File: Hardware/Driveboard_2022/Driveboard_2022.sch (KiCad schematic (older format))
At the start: 98 parts

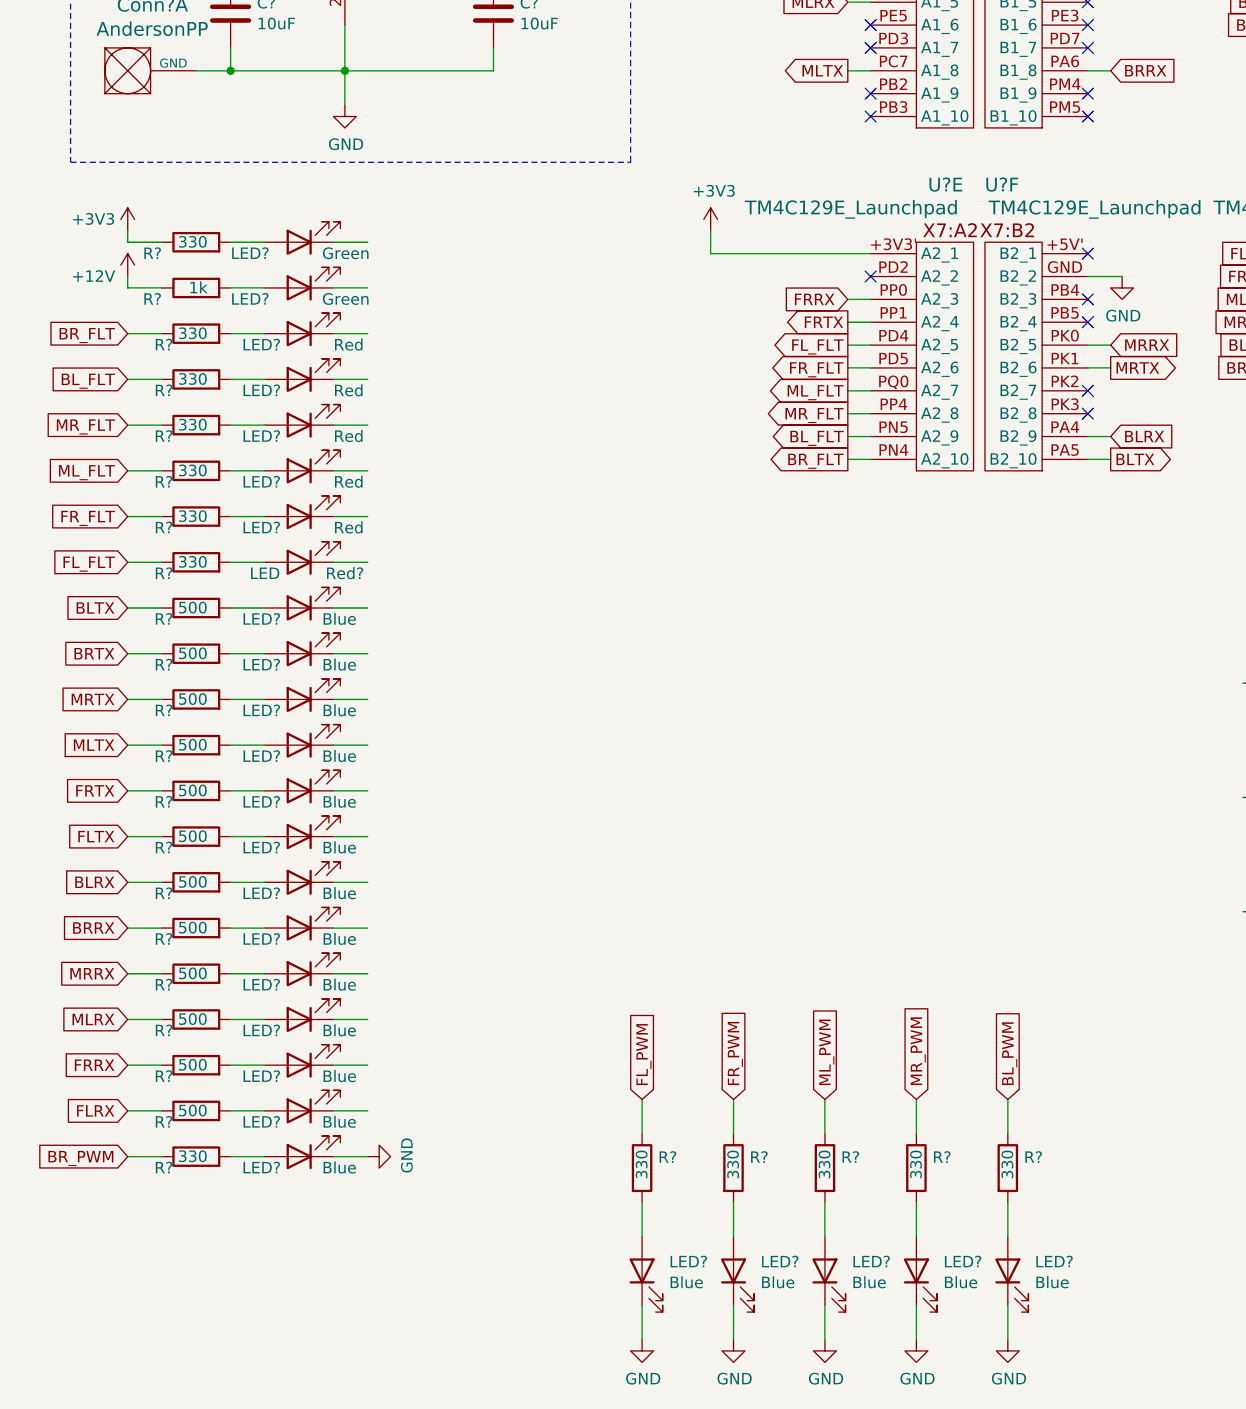
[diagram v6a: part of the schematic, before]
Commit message: Finished Organizing LEDs
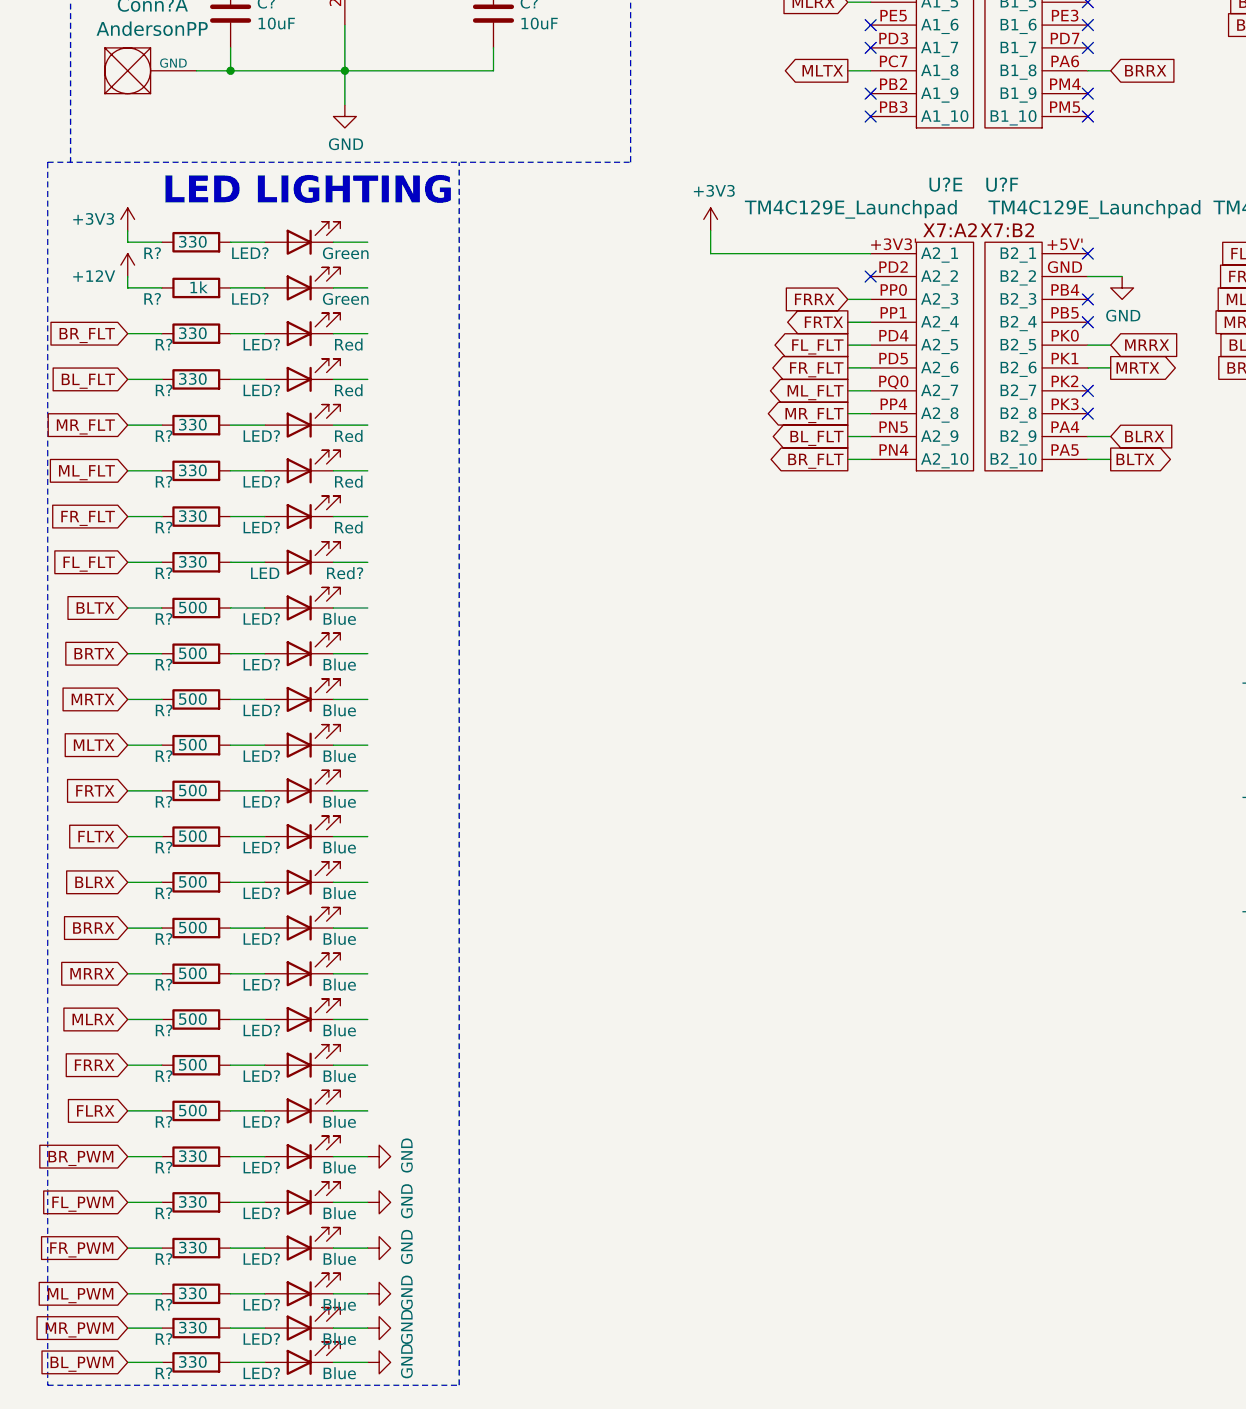
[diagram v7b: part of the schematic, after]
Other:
- note added: "LED LIGHTING\n"
- moved on the sheet: LED?, R?

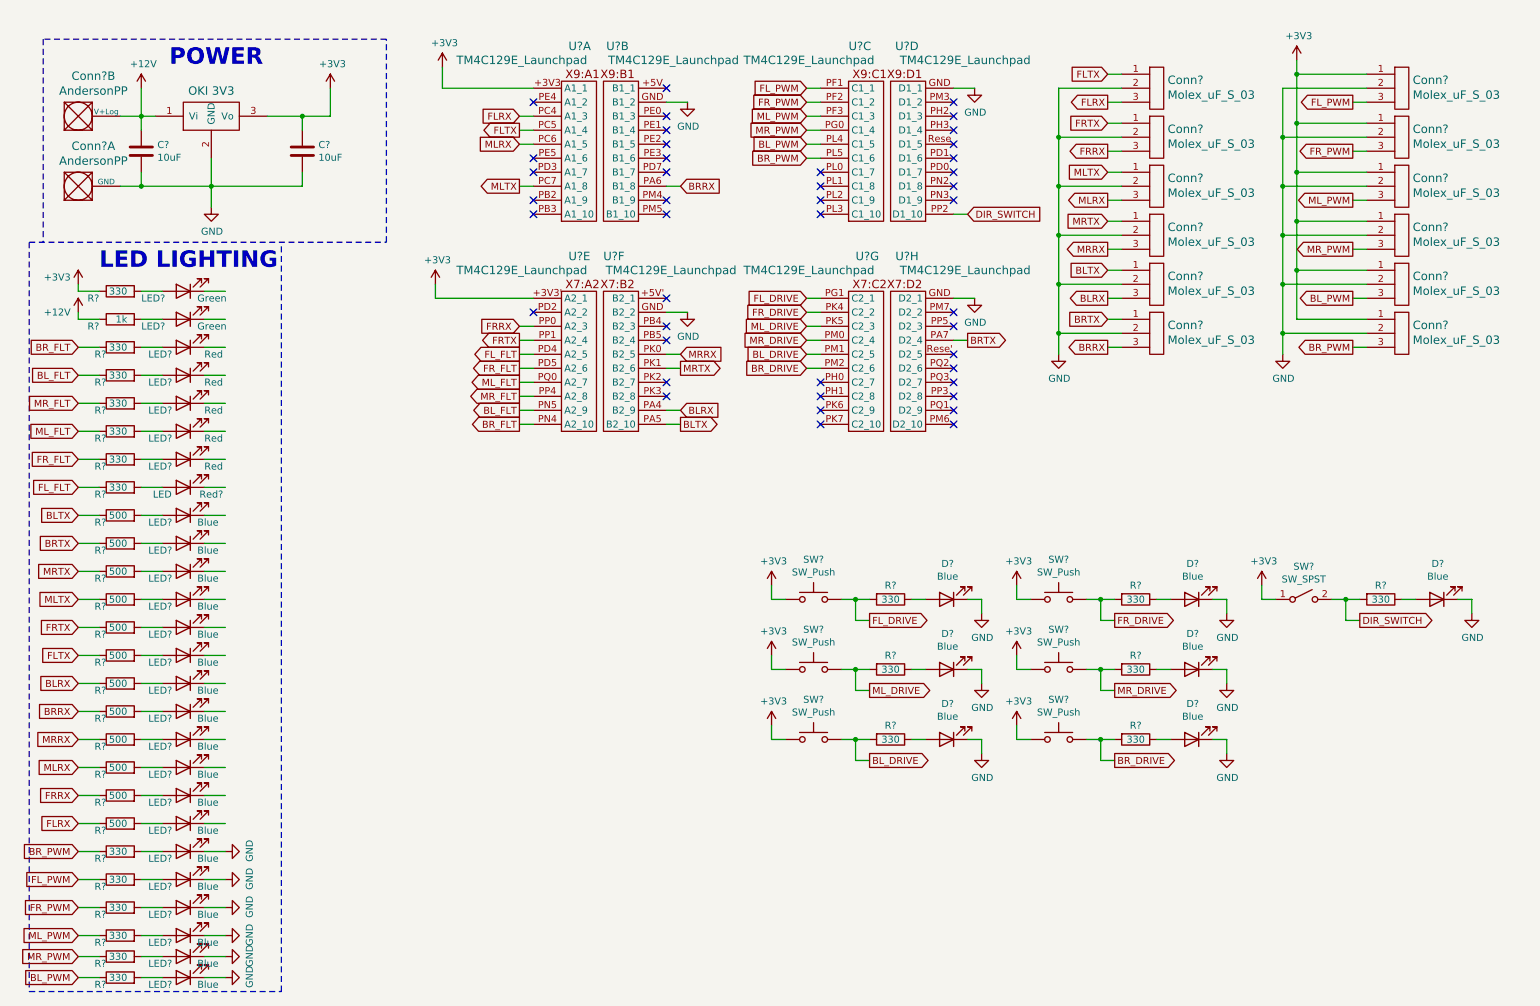
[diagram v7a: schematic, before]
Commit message: Added 5V OKI, Level Shifters, Organization
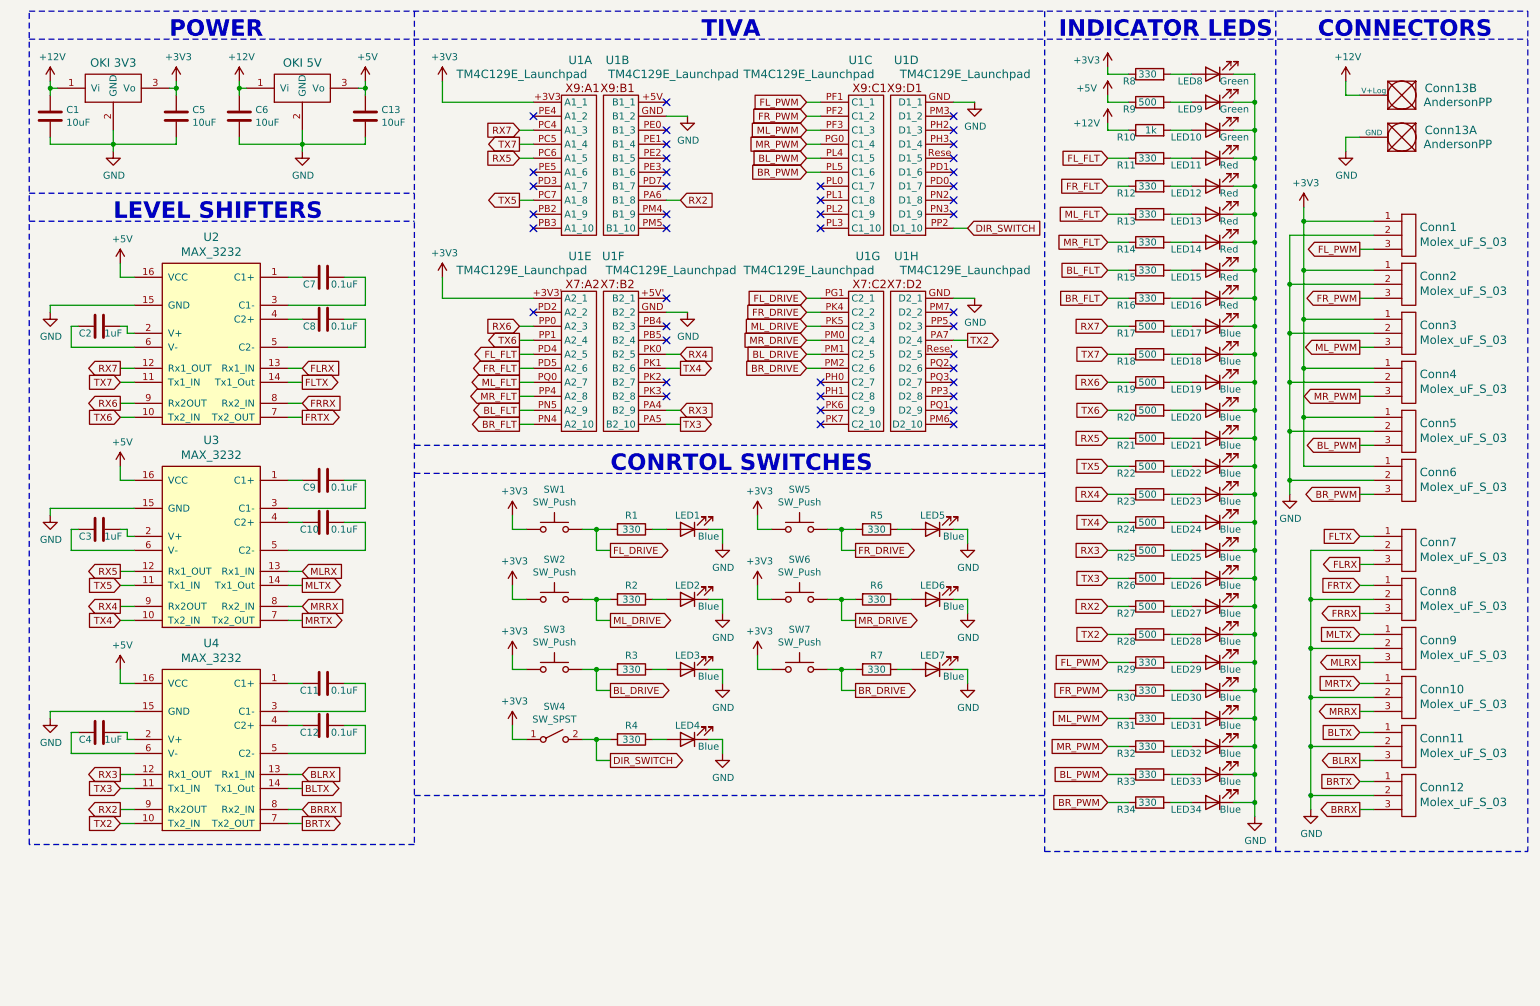
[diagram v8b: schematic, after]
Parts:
- removed Red?: LED, symbol Device:LED
- added C10, C11, C12, C7, C8, C9: 0.1uF, symbol Device:C
- added C13, C6: 10uF, symbol Device:C
- added C2, C3, C4: 1uF, symbol Device:C
- added LED16: Red, symbol Device:LED
- added LED9: Green, symbol Device:LED
- added R9: 500, symbol Device:R
- added U2, U3, U4: MAX_3232, symbol MRDT_ICs:MAX_3232
- added U6: OKI 5V, symbol MRDT_Devices:OKI
- gave numbers to parts that had none: 89
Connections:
- net labels added: +5V, RX2, RX3, RX4, RX5, RX6, RX7, TX2, TX3, TX4, TX5, TX6, TX7
- wire segments 251 -> 373
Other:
- note added: "CONNECTORS"
- note added: "CONRTOL SWITCHES"
- note added: "INDICATOR LEDS\n"
- note added: "LEVEL SHIFTERS"
- note added: "TIVA"
- note removed: "LED LIGHTING\n"
- moved on the sheet: C1, C5, Conn1, Conn10, Conn11, Conn12, Conn13A, Conn13B, Conn2, Conn3, Conn4, Conn5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
